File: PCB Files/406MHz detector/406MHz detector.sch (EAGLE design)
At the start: 30 parts, among them J1 switch, J3 select jumper, U2 ATMEGA328P_TQFP, Y1 8MHz

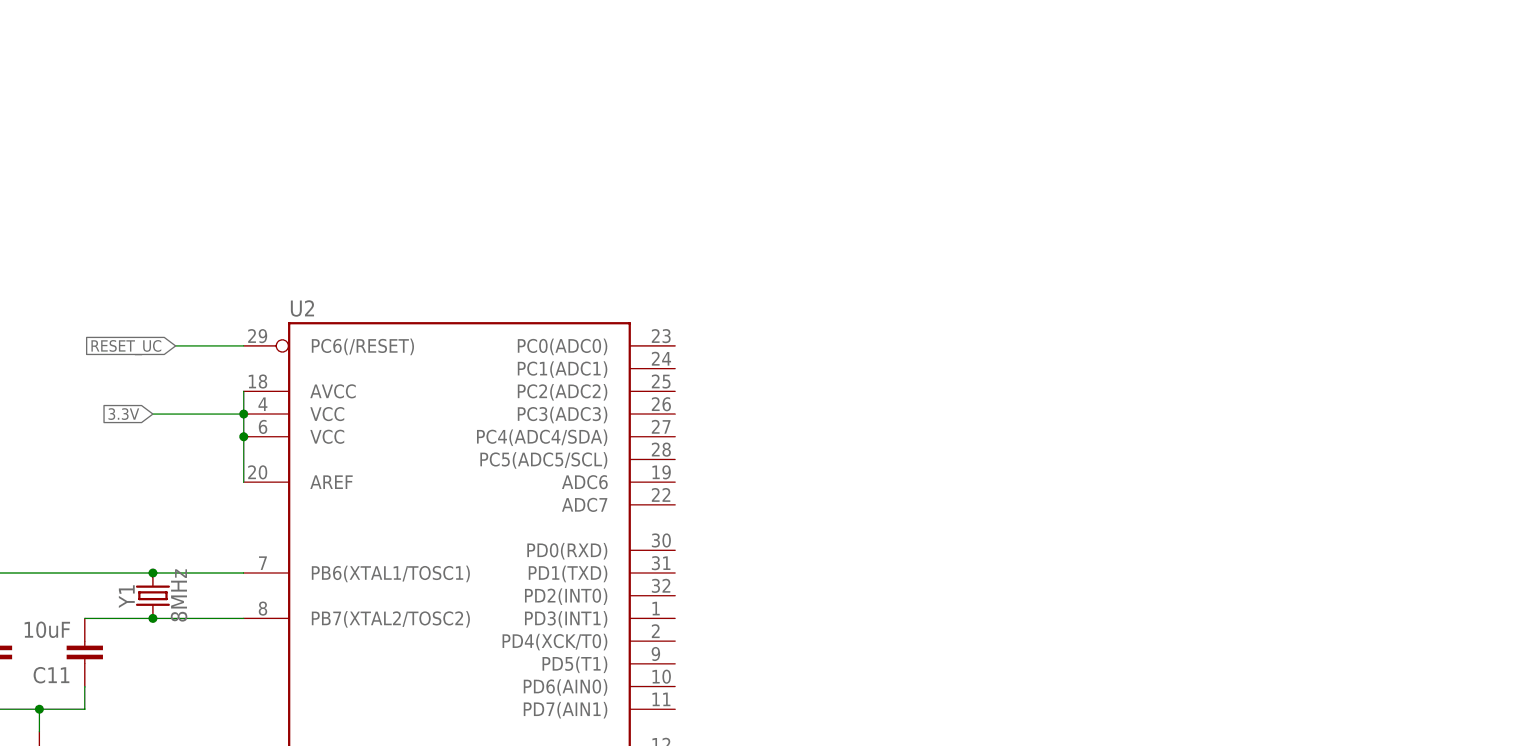
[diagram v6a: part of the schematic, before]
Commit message: components added to schematic
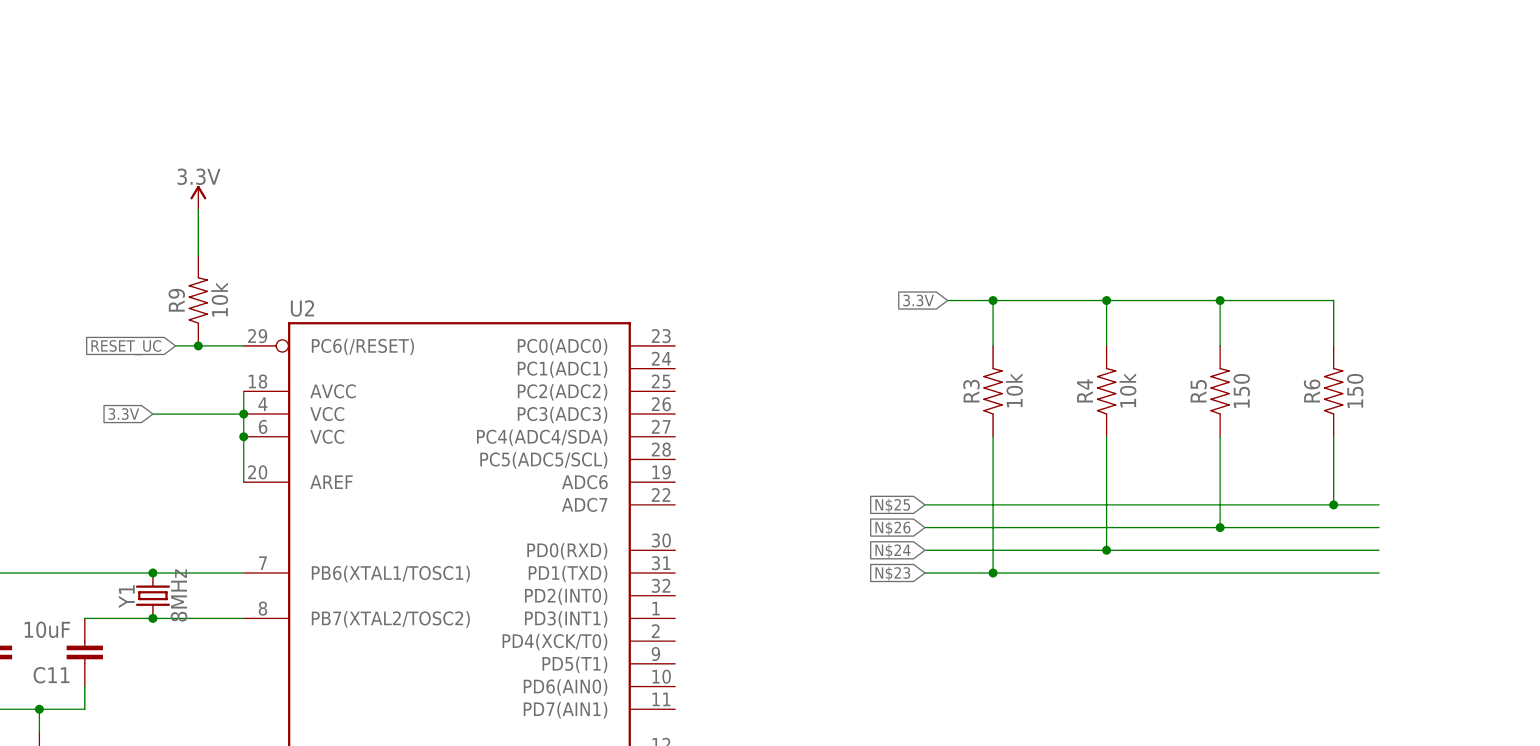
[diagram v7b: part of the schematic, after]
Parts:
- added R3, R4, R9: 10k, SparkFun-Resistors:10KOHM-0603-1/10W-1%
- added R5, R6: 150, SparkFun-Resistors:150OHM-0603-1/10W-1%
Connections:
- new net N$23: R3.1
- new net N$24: R4.1
- new net N$25: R6.1
- new net N$26: R5.1
- net 3.3V: now also R3.2, R4.2, R5.2, R6.2, R9.2
- net RESET_UC: now also R9.1
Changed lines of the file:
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@@
 <part name="C12" library="SparkFun-Capacitors" library_urn="urn:adsk.eagle:library:510" deviceset="10UF" device="-1206-6.3V-20%" package3d_urn="urn:adsk.eagle:package:37426/1" value="10uF"/>
 <part name="GND14" library="SparkFun-PowerSymbols" library_urn="urn:adsk.eagle:library:530" deviceset="GND" device=""/>
+<part name="R3" library="SparkFun-Resistors" library_urn="urn:adsk.eagle:library:532" deviceset="10KOHM" device="-0603-1/10W-1%" package3d_urn="urn:adsk.eagle:package:39650/1" value="10k"/>
+<part name="R4" library="SparkFun-Resistors" library_urn="urn:adsk.eagle:library:532" deviceset="10KOHM" device="-0603-1/10W-1%" package3d_urn="urn:adsk.eagle:package:39650/1" value="10k"/>
+<part name="R5" library="SparkFun-Resistors" library_urn="urn:adsk.eagle:library:532" deviceset="150OHM" device="-0603-1/10W-1%" package3d_urn="urn:adsk.eagle:package:39650/1" value="150"/>
+<part name="R6" library="SparkFun-Resistors" library_urn="urn:adsk.eagle:library:532" deviceset="150OHM" device="-0603-1/10W-1%" package3d_urn="urn:adsk.eagle:package:39650/1" value="150"/>
+<part name="R9" library="SparkFun-Resistors" library_urn="urn:adsk.eagle:library:532" deviceset="10KOHM" device="-0603-1/10W-1%" package3d_urn="urn:adsk.eagle:package:39650/1" value="10k"/>
+<part name="SUPPLY1" library="SparkFun-PowerSymbols" library_urn="urn:adsk.eagle:library:530" deviceset="3.3V" device=""/>
 </parts>
 <sheets>
@@
 <attribute name="VALUE" x="165.1" y="53.086" size="1.778" layer="96" align="top-center"/>
 </instance>
+<instance part="R3" gate="G$1" x="271.78" y="93.98" smashed="yes" rot="R90">
+<attribute name="NAME" x="270.256" y="93.98" size="1.778" layer="95" font="vector" rot="R90" align="bottom-center"/>
+<attribute name="VALUE" x="273.304" y="93.98" size="1.778" layer="96" font="vector" rot="R90" align="top-center"/>
+</instance>
+<instance part="R4" gate="G$1" x="284.48" y="93.98" smashed="yes" rot="R90">
+<attribute name="NAME" x="282.956" y="93.98" size="1.778" layer="95" font="vector" rot="R90" align="bottom-center"/>
+<attribute name="VALUE" x="286.004" y="93.98" size="1.778" layer="96" font="vector" rot="R90" align="top-center"/>
+</instance>
+<instance part="R5" gate="G$1" x="297.18" y="93.98" smashed="yes" rot="R90">
+<attribute name="NAME" x="295.656" y="93.98" size="1.778" layer="95" font="vector" rot="R90" align="bottom-center"/>
+<attribute name="VALUE" x="298.704" y="93.98" size="1.778" layer="96" font="vector" rot="R90" align="top-center"/>
+</instance>
+<instance part="R6" gate="G$1" x="309.88" y="93.98" smashed="yes" rot="R90">
+<attribute name="NAME" x="308.356" y="93.98" size="1.778" layer="95" font="vector" rot="R90" align="bottom-center"/>
+<attribute name="VALUE" x="311.404" y="93.98" size="1.778" layer="96" font="vector" rot="R90" align="top-center"/>
+</instance>
+<instance part="R9" gate="G$1" x="182.88" y="104.14" smashed="yes" rot="R90">
+<attribute name="NAME" x="181.356" y="104.14" size="1.778" layer="95" font="vector" rot="R90" align="bottom-center"/>
+<attribute name="VALUE" x="184.404" y="104.14" size="1.778" layer="96" font="vector" rot="R90" align="top-center"/>
+</instance>
+<instance part="SUPPLY1" gate="G$1" x="182.88" y="114.3" smashed="yes">
+<attribute name="VALUE" x="182.88" y="117.094" size="1.778" layer="96" align="bottom-center"/>
+</instance>
 </instances>
 <busses>
@@
 <junction x="187.96" y="88.9"/>
 </segment>
+<segment>
+<pinref part="R4" gate="G$1" pin="2"/>
+<wire x1="284.48" y1="99.06" x2="284.48" y2="104.14" width="0.1524" layer="91"/>
+<wire x1="284.48" y1="104.14" x2="271.78" y2="104.14" width="0.1524" layer="91"/>
+<pinref part="R3" gate="G$1" pin="2"/>
+<wire x1="271.78" y1="104.14" x2="271.78" y2="99.06" width="0.1524" layer="91"/>
+<wire x1="271.78" y1="104.14" x2="266.7" y2="104.14" width="0.1524" layer="91"/>
+<junction x="271.78" y="104.14"/>
+<label x="266.7" y="104.14" size="1.27" layer="95" rot="R180" xref="yes"/>
+<pinref part="R5" gate="G$1" pin="2"/>
+<wire x1="297.18" y1="99.06" x2="297.18" y2="104.14" width="0.1524" layer="91"/>
+<pinref part="R6" gate="G$1" pin="2"/>
+<wire x1="297.18" y1="104.14" x2="309.88" y2="104.14" width="0.1524" layer="91"/>
+<wire x1="309.88" y1="104.14" x2="309.88" y2="99.06" width="0.1524" layer="91"/>
+<wire x1="297.18" y1="104.14" x2="284.48" y2="104.14" width="0.1524" layer="91"/>
+<junction x="297.18" y="104.14"/>
+<junction x="284.48" y="104.14"/>
+</segment>
+<segment>
+<pinref part="R9" gate="G$1" pin="2"/>
+<wire x1="182.88" y1="109.22" x2="182.88" y2="114.3" width="0.1524" layer="91"/>
+<pinref part="SUPPLY1" gate="G$1" pin="3.3V"/>
+</segment>
 </net>
 <net name="N$2" class="0">
@@
 <segment>
 <pinref part="U2" gate="U$1" pin="PC6(/RESET)"/>
-<wire x1="187.96" y1="99.06" x2="180.34" y2="99.06" width="0.1524" layer="91"/>
+<wire x1="187.96" y1="99.06" x2="182.88" y2="99.06" width="0.1524" layer="91"/>
 <label x="180.34" y="99.06" size="1.27" layer="95" rot="R180" xref="yes"/>
+<pinref part="R9" gate="G$1" pin="1"/>
+<wire x1="182.88" y1="99.06" x2="180.34" y2="99.06" width="0.1524" layer="91"/>
+<junction x="182.88" y="99.06"/>
 </segment>
 </net>
@@
 </segment>
 </net>
+<net name="N$23" class="0">
+<segment>
+<pinref part="R3" gate="G$1" pin="1"/>
+<wire x1="271.78" y1="88.9" x2="271.78" y2="73.66" width="0.1524" layer="91"/>
+<wire x1="271.78" y1="73.66" x2="314.96" y2="73.66" width="0.1524" layer="91"/>
+<wire x1="271.78" y1="73.66" x2="264.16" y2="73.66" width="0.1524" layer="91"/>
+<junction x="271.78" y="73.66"/>
+<label x="264.16" y="73.66" size="1.27" layer="95" rot="R180" xref="yes"/>
+</segment>
+</net>
+<net name="N$24" class="0">
+<segment>
+<pinref part="R4" gate="G$1" pin="1"/>
+<wire x1="284.48" y1="88.9" x2="284.48" y2="76.2" width="0.1524" layer="91"/>
+<wire x1="284.48" y1="76.2" x2="314.96" y2="76.2" width="0.1524" layer="91"/>
+<wire x1="284.48" y1="76.2" x2="264.16" y2="76.2" width="0.1524" layer="91"/>
+<junction x="284.48" y="76.2"/>
+<label x="264.16" y="76.2" size="1.27" layer="95" rot="R180" xref="yes"/>
+</segment>
+</net>
+<net name="N$26" class="0">
+<segment>
+<pinref part="R5" gate="G$1" pin="1"/>
+<wire x1="297.18" y1="88.9" x2="297.18" y2="78.74" width="0.1524" layer="91"/>
+<wire x1="297.18" y1="78.74" x2="314.96" y2="78.74" width="0.1524" layer="91"/>
+<wire x1="297.18" y1="78.74" x2="264.16" y2="78.74" width="0.1524" layer="91"/>
+<junction x="297.18" y="78.74"/>
+<label x="264.16" y="78.74" size="1.27" layer="95" rot="R180" xref="yes"/>
+</segment>
+</net>
+<net name="N$25" class="0">
+<segment>
+<pinref part="R6" gate="G$1" pin="1"/>
+<wire x1="309.88" y1="88.9" x2="309.88" y2="81.28" width="0.1524" layer="91"/>
+<wire x1="309.88" y1="81.28" x2="314.96" y2="81.28" width="0.1524" layer="91"/>
+<wire x1="309.88" y1="81.28" x2="264.16" y2="81.28" width="0.1524" layer="91"/>
+<junction x="309.88" y="81.28"/>
+<label x="264.16" y="81.28" size="1.27" layer="95" rot="R180" xref="yes"/>
+</segment>
+</net>
